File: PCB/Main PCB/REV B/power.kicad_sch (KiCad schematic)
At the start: 16 parts, among them U5 TPS2115APWR, U6 AMS1117-3.3

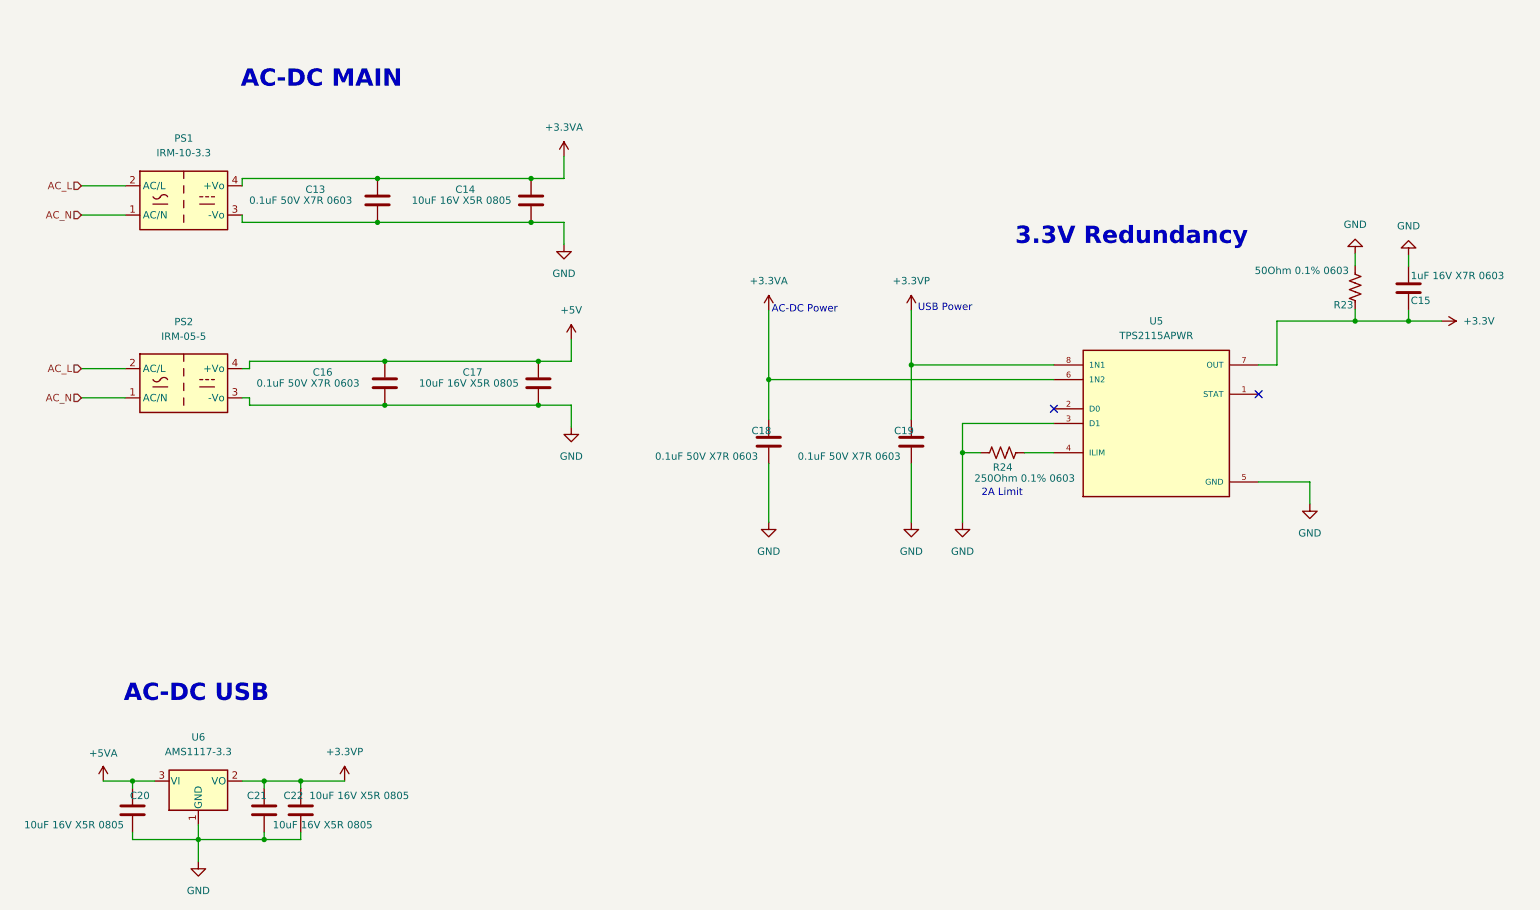
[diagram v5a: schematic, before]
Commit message: PCB schematic updates, Changed transistor on reboot to double
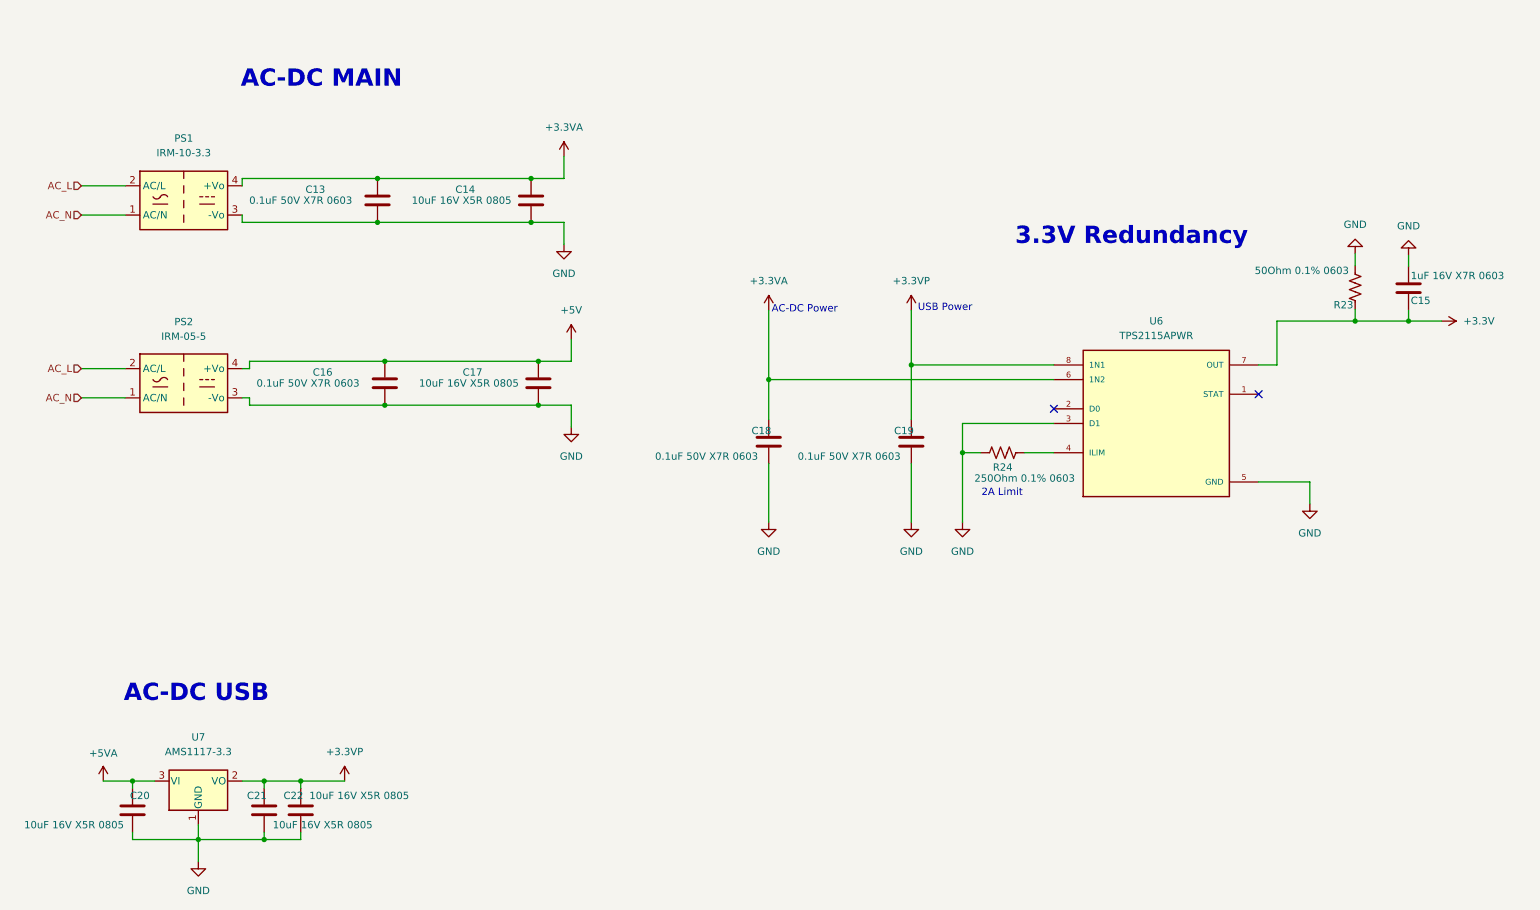
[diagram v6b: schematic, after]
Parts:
- renumbered U5 to U6, U6 to U7
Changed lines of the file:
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@@
   (symbol (lib_id "TPS2115APWR:TPS2115APWR") (at 218.694 92.329 0) (unit 1)
     (in_bom yes) (on_board yes) (fields_autoplaced)
-    (property "Reference" "U5" (id 0) (at 218.694 74.549 0))
+    (property "Reference" "U6" (id 0) (at 218.694 74.549 0))
     (property "Value" "TPS2115APWR" (id 1) (at 218.694 77.089 0))
     (property "Footprint" "Customs Smoker:PW8-M" (id 2) (at 218.694 92.329 0)
@@
   (symbol (lib_id "power:+3.3VP") (at 176.149 72.644 0) (unit 1)
     (in_bom yes) (on_board yes) (fields_autoplaced)
-    (property "Reference" "#PWR057" (id 0) (at 179.959 73.914 0)
+    (property "Reference" "#PWR059" (id 0) (at 179.959 73.914 0)
       (effects (font (size 1.27 1.27)) hide)
     )
@@
   (symbol (lib_id "power:GND") (at 52.324 168.402 0) (unit 1)
     (in_bom yes) (on_board yes)
-    (property "Reference" "#PWR067" (id 0) (at 52.324 174.752 0)
+    (property "Reference" "#PWR069" (id 0) (at 52.324 174.752 0)
       (effects (font (size 1.27 1.27)) hide)
     )
@@
   (symbol (lib_id "power:GND") (at 151.384 109.474 0) (unit 1)
     (in_bom yes) (on_board yes) (fields_autoplaced)
-    (property "Reference" "#PWR062" (id 0) (at 151.384 115.824 0)
+    (property "Reference" "#PWR064" (id 0) (at 151.384 115.824 0)
       (effects (font (size 1.27 1.27)) hide)
     )
@@
   (symbol (lib_id "power:GND") (at 185.039 109.474 0) (unit 1)
     (in_bom yes) (on_board yes) (fields_autoplaced)
-    (property "Reference" "#PWR064" (id 0) (at 185.039 115.824 0)
+    (property "Reference" "#PWR066" (id 0) (at 185.039 115.824 0)
       (effects (font (size 1.27 1.27)) hide)
     )
@@
   (symbol (lib_id "power:+3.3V") (at 268.224 74.549 270) (unit 1)
     (in_bom yes) (on_board yes) (fields_autoplaced)
-    (property "Reference" "#PWR058" (id 0) (at 264.414 74.549 0)
+    (property "Reference" "#PWR060" (id 0) (at 264.414 74.549 0)
       (effects (font (size 1.27 1.27)) hide)
     )
@@
   (symbol (lib_id "power:GND") (at 117.094 92.964 0) (unit 1)
     (in_bom yes) (on_board yes)
-    (property "Reference" "#PWR060" (id 0) (at 117.094 99.314 0)
+    (property "Reference" "#PWR062" (id 0) (at 117.094 99.314 0)
       (effects (font (size 1.27 1.27)) hide)
     )
@@
   (symbol (lib_id "power:+3.3VA") (at 151.384 72.644 0) (unit 1)
     (in_bom yes) (on_board yes) (fields_autoplaced)
-    (property "Reference" "#PWR056" (id 0) (at 151.384 76.454 0)
+    (property "Reference" "#PWR058" (id 0) (at 151.384 76.454 0)
       (effects (font (size 1.27 1.27)) hide)
     )
@@
   (symbol (lib_id "power:GND") (at 115.824 61.214 0) (unit 1)
     (in_bom yes) (on_board yes)
-    (property "Reference" "#PWR053" (id 0) (at 115.824 67.564 0)
+    (property "Reference" "#PWR055" (id 0) (at 115.824 67.564 0)
       (effects (font (size 1.27 1.27)) hide)
     )
@@
   (symbol (lib_id "power:GND") (at 253.238 62.865 180) (unit 1)
     (in_bom yes) (on_board yes) (fields_autoplaced)
-    (property "Reference" "#PWR054" (id 0) (at 253.238 56.515 0)
+    (property "Reference" "#PWR056" (id 0) (at 253.238 56.515 0)
       (effects (font (size 1.27 1.27)) hide)
     )
@@
   (symbol (lib_id "power:+3.3VP") (at 77.724 154.432 0) (unit 1)
     (in_bom yes) (on_board yes) (fields_autoplaced)
-    (property "Reference" "#PWR066" (id 0) (at 81.534 155.702 0)
+    (property "Reference" "#PWR068" (id 0) (at 81.534 155.702 0)
       (effects (font (size 1.27 1.27)) hide)
     )
@@
   (symbol (lib_id "power:GND") (at 262.509 63.119 180) (unit 1)
     (in_bom yes) (on_board yes) (fields_autoplaced)
-    (property "Reference" "#PWR055" (id 0) (at 262.509 56.769 0)
+    (property "Reference" "#PWR057" (id 0) (at 262.509 56.769 0)
       (effects (font (size 1.27 1.27)) hide)
     )
@@
   (symbol (lib_id "Regulator_Linear:AMS1117-3.3") (at 52.324 154.432 0) (unit 1)
     (in_bom yes) (on_board yes) (fields_autoplaced)
-    (property "Reference" "U6" (id 0) (at 52.324 146.812 0))
+    (property "Reference" "U7" (id 0) (at 52.324 146.812 0))
     (property "Value" "AMS1117-3.3" (id 1) (at 52.324 149.352 0))
     (property "Footprint" "Package_TO_SOT_SMD:TO-252-2" (id 2) (at 52.324 149.352 0)
@@
   (symbol (lib_id "power:+5VA") (at 35.814 154.432 0) (unit 1)
     (in_bom yes) (on_board yes) (fields_autoplaced)
-    (property "Reference" "#PWR065" (id 0) (at 35.814 158.242 0)
+    (property "Reference" "#PWR067" (id 0) (at 35.814 158.242 0)
       (effects (font (size 1.27 1.27)) hide)
     )
@@
   (symbol (lib_id "power:GND") (at 245.364 106.299 0) (unit 1)
     (in_bom yes) (on_board yes) (fields_autoplaced)
-    (property "Reference" "#PWR061" (id 0) (at 245.364 112.649 0)
+    (property "Reference" "#PWR063" (id 0) (at 245.364 112.649 0)
       (effects (font (size 1.27 1.27)) hide)
     )
@@
   (symbol (lib_id "power:+5V") (at 117.094 77.724 0) (unit 1)
     (in_bom yes) (on_board yes) (fields_autoplaced)
-    (property "Reference" "#PWR059" (id 0) (at 117.094 81.534 0)
+    (property "Reference" "#PWR061" (id 0) (at 117.094 81.534 0)
       (effects (font (size 1.27 1.27)) hide)
     )
@@
   (symbol (lib_id "power:GND") (at 176.149 109.474 0) (unit 1)
     (in_bom yes) (on_board yes) (fields_autoplaced)
-    (property "Reference" "#PWR063" (id 0) (at 176.149 115.824 0)
+    (property "Reference" "#PWR065" (id 0) (at 176.149 115.824 0)
       (effects (font (size 1.27 1.27)) hide)
     )
@@
   (symbol (lib_id "power:+3.3VA") (at 115.824 45.974 0) (unit 1)
     (in_bom yes) (on_board yes) (fields_autoplaced)
-    (property "Reference" "#PWR052" (id 0) (at 115.824 49.784 0)
-      (effects (font (size 1.27 1.27)) hide)
-    )
+    (property "Reference" "#PWR054" (id 0) (at 115.824 49.784 0)
+      (effects (font (size 1.27 1.27)) hide)
+    )
